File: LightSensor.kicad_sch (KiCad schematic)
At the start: 7 parts, among them U5 OPT4003DNPRQ1

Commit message: v3.1 Updates
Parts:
- removed R102, R103: 0R, Resistor_SMD:R_0603_1608Metric, symbol Device:R_Small
- C1: renamed from C36; value 0.1uF -> 100n
- R1: renamed from R104; now not fitted
- R2: renamed from R105; now not fitted
- renumbered U5 to U1
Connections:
- net ADDR_LS renamed ADDR
- net PERI_3V3 renamed 3V3_P
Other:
- sheet I2C Single Protection2 renamed I2C Single Protection
- sheet I2C Single Protection3 renamed I2C Single Protection1
- note added: "I2C ADDR Install R1: 0x45 Install R2: 0x44"
- note removed: "I2C ADDR Install R34: 0x45 Install R35: 0x44"
- company: (none) -> Carnegie Mellon University
- title: (none) -> Argus XY Solar Panel
- moved on the sheet: C1, F1, U1

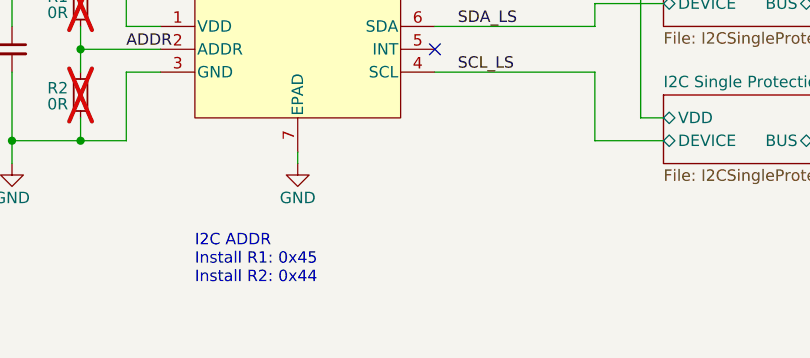
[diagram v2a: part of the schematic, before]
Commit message: Updated access port, added deployment sensor
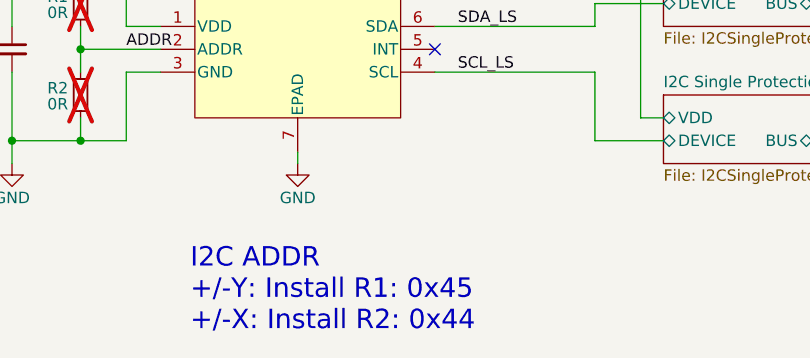
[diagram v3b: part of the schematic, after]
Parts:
- C1: MPN (none) -> C307348
- U1: MPN (none) -> C22406808
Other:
- note added: "I2C ADDR +/-Y: Install R1: 0x45 +/-X: Install R2: 0x44"
- note removed: "I2C ADDR Install R1: 0x45 Install R2: 0x44"
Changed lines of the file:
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@@
 		(comment 2 "V. Rajesh")
 	)
-	(text "I2C ADDR\nInstall R1: 0x45\nInstall R2: 0x44"
+	(text "I2C ADDR\n+/-Y: Install R1: 0x45\n+/-X: Install R2: 0x44"
 		(exclude_from_sim no)
-		(at 129.54 123.952 0)
+		(at 129.032 129.286 0)
 		(effects
 			(font
-				(size 1.27 1.27)
+				(size 2.159 2.159)
 			)
 			(justify left bottom)
@@
 			)
 		)
+		(property "MPN" "C22406808"
+			(at 140.97 97.79 0)
+			(effects
+				(font
+					(size 1.27 1.27)
+				)
+				(hide yes)
+			)
+		)
 		(pin "6"
 		)
@@
 			(at 109.22 97.79 0)
 			(effects
+				(font
+					(size 1.27 1.27)
+				)
+				(hide yes)
+			)
+		)
+		(property "MPN" "C307348"
+			(at 109.22 97.79 0)
+			(effects

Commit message: Local Stash
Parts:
- R1, R2: now fitted
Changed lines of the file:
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@@
 		(in_bom yes)
 		(on_board yes)
-		(dnp yes)
+		(dnp no)
 		(property "Reference" "R1"
 			(at 114.3 91.948 0)
@@
 		(in_bom yes)
 		(on_board yes)
-		(dnp yes)
+		(dnp no)
 		(property "Reference" "R2"
 			(at 114.3 102.108 0)
